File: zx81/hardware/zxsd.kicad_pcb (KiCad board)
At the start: 2 copper layers, 69.9 x 95.9 mm, 36 parts, among them J1 Micro_SD_Card, J2 ZX81_EXP, SW1 RESET, U1 74HCT32, U10 27C256, U11 KM62256CLP, U2 74HCT32, U3 74HCT00, U4 74HCT02, U5 74HCT163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

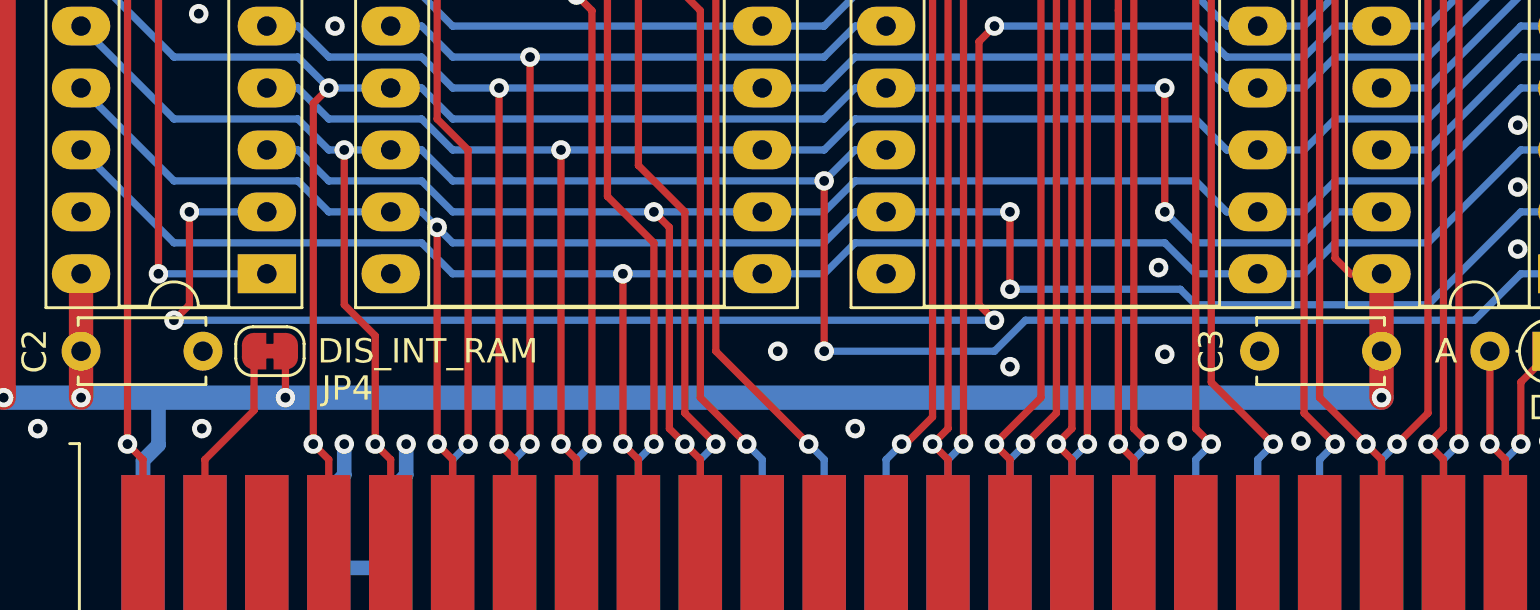
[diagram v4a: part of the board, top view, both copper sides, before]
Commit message: use real jumper for dis_int_ram
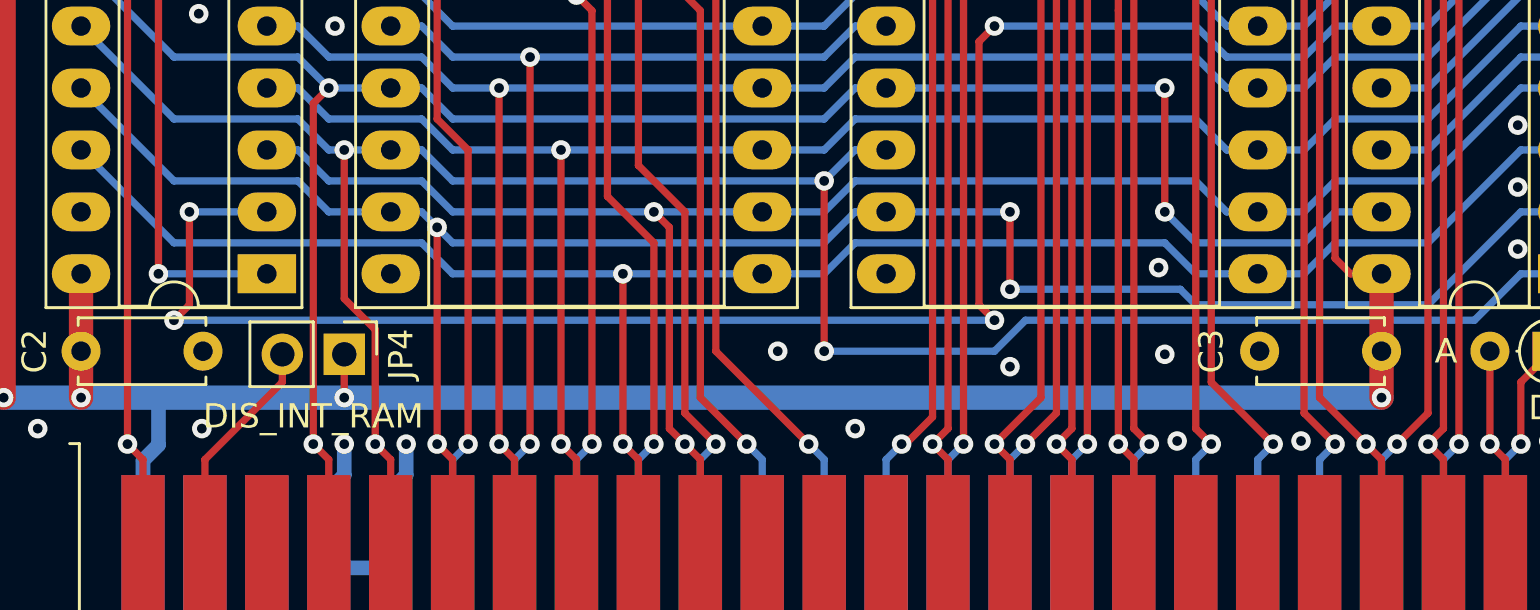
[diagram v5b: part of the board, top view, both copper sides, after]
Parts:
- JP4: footprint Jumper:SolderJumper-2_P1.3mm_Bridged_RoundedPad1.0x1.5mm -> Connector_PinHeader_2.54mm:PinHeader_1x02_P2.54mm_Vertical
- moved JP4 3.05 mm to (127.6, 126.5), turned to 270 degrees
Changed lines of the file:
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@@
     (add_net "Net-(J1-Pad5)")
     (add_net "Net-(J1-Pad8)")
+    (add_net "Net-(J2-Pad11a)")
+    (add_net "Net-(J2-Pad12a)")
+    (add_net "Net-(J2-Pad13a)")
+    (add_net "Net-(J2-Pad18a)")
+    (add_net "Net-(J2-Pad19a)")
+    (add_net "Net-(J2-Pad20a)")
+    (add_net "Net-(J2-Pad2b)")
+    (add_net "Net-(J2-Pad3a)")
+    (add_net "Net-(J2-Pad3b)")
     (add_net "Net-(JP1-Pad1)")
     (add_net "Net-(JP1-Pad3)")
@@
     (add_net "Net-(U11-Pad1)")
     (add_net "Net-(U2-Pad10)")
+    (add_net "Net-(U2-Pad11)")
     (add_net "Net-(U2-Pad4)")
     (add_net "Net-(U2-Pad8)")
     (add_net "Net-(U2-Pad9)")
     (add_net "Net-(U4-Pad1)")
+    (add_net "Net-(U4-Pad10)")
+    (add_net "Net-(U5-Pad13)")
+    (add_net "Net-(U5-Pad14)")
+    (add_net "Net-(U5-Pad15)")
+    (add_net "Net-(U6-Pad7)")
+    (add_net "Net-(U7-Pad9)")
+    (add_net "Net-(U8-Pad8)")
+  )
+  (module Connector_PinHeader_2.54mm:PinHeader_1x02_P2.54mm_Vertical (layer F.Cu)
+    (at 127.635 126.492 270)
+    (descr "Through hole straight pin header, 1x02, 2.54mm pitch, single row")
+    (tags "Through hole pin header THT 1x02 2.54mm single row")
+    (fp_text reference JP4 (at 0 -2.33 90) (layer F.SilkS)
+      (effects (font (size 1 1) (thickness 0.15)))
+    )
+    (fp_text value DIS_INT_RAM (at 0 4.87 90) (layer F.Fab)
+      (effects (font (size 1 1) (thickness 0.15)))
+    )
+    (fp_line (start 1.8 -1.8) (end -1.8 -1.8) (layer F.CrtYd) (width 0.05))
+    (fp_line (start 1.8 4.35) (end 1.8 -1.8) (layer F.CrtYd) (width 0.05))
+    (fp_line (start -1.8 4.35) (end 1.8 4.35) (layer F.CrtYd) (width 0.05))
+    (fp_line (start -1.8 -1.8) (end -1.8 4.35) (layer F.CrtYd) (width 0.05))
+    (fp_line (start -1.33 -1.33) (end 0 -1.33) (layer F.SilkS) (width 0.12))
+    (fp_line (start -1.33 0) (end -1.33 -1.33) (layer F.SilkS) (width 0.12))
+    (fp_line (start -1.33 1.27) (end 1.33 1.27) (layer F.SilkS) (width 0.12))
+    (fp_line (start 1.33 1.27) (end 1.33 3.87) (layer F.SilkS) (width 0.12))
+    (fp_line (start -1.33 1.27) (end -1.33 3.87) (layer F.SilkS) (width 0.12))
+    (fp_line (start -1.33 3.87) (end 1.33 3.87) (layer F.SilkS) (width 0.12))
+    (fp_line (start -1.27 -0.635) (end -0.635 -1.27) (layer F.Fab) (width 0.1))
+    (fp_line (start -1.27 3.81) (end -1.27 -0.635) (layer F.Fab) (width 0.1))
+    (fp_line (start 1.27 3.81) (end -1.27 3.81) (layer F.Fab) (width 0.1))
+    (fp_line (start 1.27 -1.27) (end 1.27 3.81) (layer F.Fab) (width 0.1))
+    (fp_line (start -0.635 -1.27) (end 1.27 -1.27) (layer F.Fab) (width 0.1))
+    (fp_text user %R (at 0 1.27) (layer F.Fab)
+      (effects (font (size 1 1) (thickness 0.15)))
+    )
+    (pad 2 thru_hole oval (at 0 2.54 270) (size 1.7 1.7) (drill 1) (layers *.Cu *.Mask)
+      (net 50 /nRAMCS_INT))
+    (pad 1 thru_hole rect (at 0 0 270) (size 1.7 1.7) (drill 1) (layers *.Cu *.Mask)
+      (net 1 +5V))
+    (model ${KISYS3DMOD}/Connector_PinHeader_2.54mm.3dshapes/PinHeader_1x02_P2.54mm_Vertical.wrl
+      (at (xyz 0 0 0))
+      (scale (xyz 1 1 1))
+      (rotate (xyz 0 0 0))
+    )
   )
   (module Package_DIP:DIP-14_W7.62mm_Socket_LongPads (layer F.Cu)
@@
     )
   )
-  (module Jumper:SolderJumper-2_P1.3mm_Bridged_RoundedPad1.0x1.5mm (layer F.Cu)
-    (at 124.587 126.365 180)
-    (descr "SMD Solder Jumper, 1x1.5mm, rounded Pads, 0.3mm gap, bridged with 1 copper strip")
-    (tags "solder jumper open")
-    (attr virtual)
-    (fp_text reference JP4 (at -3.175 -1.524) (layer F.SilkS)
-      (effects (font (size 1 1) (thickness 0.15)))
-    )
-    (fp_text value DIS_INT_RAM (at 0 1.9) (layer F.Fab)
-      (effects (font (size 1 1) (thickness 0.15)))
-    )
-    (fp_poly (pts (xy 0.25 -0.3) (xy -0.25 -0.3) (xy -0.25 0.3) (xy 0.25 0.3)) (layer F.Cu) (width 0))
-    (fp_line (start 1.65 1.25) (end -1.65 1.25) (layer F.CrtYd) (width 0.05))
-    (fp_line (start 1.65 1.25) (end 1.65 -1.25) (layer F.CrtYd) (width 0.05))
-    (fp_line (start -1.65 -1.25) (end -1.65 1.25) (layer F.CrtYd) (width 0.05))
-    (fp_line (start -1.65 -1.25) (end 1.65 -1.25) (layer F.CrtYd) (width 0.05))
-    (fp_line (start -0.7 -1) (end 0.7 -1) (layer F.SilkS) (width 0.12))
-    (fp_line (start 1.4 -0.3) (end 1.4 0.3) (layer F.SilkS) (width 0.12))
-    (fp_line (start 0.7 1) (end -0.7 1) (layer F.SilkS) (width 0.12))
-    (fp_line (start -1.4 0.3) (end -1.4 -0.3) (layer F.SilkS) (width 0.12))
-    (fp_arc (start -0.7 -0.3) (end -0.7 -1) (angle -90) (layer F.SilkS) (width 0.12))
-    (fp_arc (start -0.7 0.3) (end -1.4 0.3) (angle -90) (layer F.SilkS) (width 0.12))
-    (fp_arc (start 0.7 0.3) (end 0.7 1) (angle -90) (layer F.SilkS) (width 0.12))
-    (fp_arc (start 0.7 -0.3) (end 1.4 -0.3) (angle -90) (layer F.SilkS) (width 0.12))
-    (pad 1 smd custom (at -0.65 0 180) (size 1 0.5) (layers F.Cu F.Mask)
-      (net 1 +5V) (zone_connect 2)
-      (options (clearance outline) (anchor rect))
-      (primitives
-        (gr_circle (center 0 0.25) (end 0.5 0.25) (width 0))
-        (gr_circle (center 0 -0.25) (end 0.5 -0.25) (width 0))
-        (gr_poly (pts
-           (xy 0 -0.75) (xy 0.5 -0.75) (xy 0.5 0.75) (xy 0 0.75)) (width 0))
-      ))
-    (pad 2 smd custom (at 0.65 0 180) (size 1 0.5) (layers F.Cu F.Mask)
-      (net 50 /nRAMCS_INT) (zone_connect 2)
-      (options (clearance outline) (anchor rect))
-      (primitives
-        (gr_circle (center 0 0.25) (end 0.5 0.25) (width 0))
-        (gr_circle (center 0 -0.25) (end 0.5 -0.25) (width 0))
-        (gr_poly (pts
-           (xy 0 -0.75) (xy -0.5 -0.75) (xy -0.5 0.75) (xy 0 0.75)) (width 0))
-      ))
-  )
   (module Package_TO_SOT_THT:TO-92_Inline (layer F.Cu)
     (at 128.27 48.26)
@@
   )
   (gr_circle (center 165.735 48.895) (end 165.935 48.895) (layer F.SilkS) (width 0.15))
-  (gr_text DIS_INT_RAM (at 131.064 126.365) (layer F.SilkS)
+  (gr_text DIS_INT_RAM (at 126.365 129.032) (layer F.SilkS)
     (effects (font (size 1 1) (thickness 0.15)))
   )
@@
   (segment (start 128.905 50.8) (end 129.54 50.165) (width 0.6) (layer B.Cu) (net 1))
   (segment (start 113.665 128.27) (end 113.665 90.17) (width 1) (layer F.Cu) (net 1))
-  (segment (start 125.222 128.27) (end 170.18 128.27) (width 1) (layer B.Cu) (net 1))
-  (via (at 125.222 128.27) (size 0.8) (drill 0.4) (layers F.Cu B.Cu) (net 1))
-  (segment (start 120.015 128.27) (end 125.222 128.27) (width 1) (layer B.Cu) (net 1))
-  (segment (start 125.222 126.38) (end 125.237 126.365) (width 0.3) (layer F.Cu) (net 1))
-  (segment (start 125.222 128.27) (end 125.222 126.38) (width 0.3) (layer F.Cu) (net 1))
   (segment (start 116.84 69.85) (end 122.555 69.85) (width 0.3) (layer B.Cu) (net 1))
   (via (at 122.555 69.85) (size 0.8) (drill 0.4) (layers F.Cu B.Cu) (net 1))
@@
   (via (at 165.1 85.09) (size 0.8) (drill 0.4) (layers F.Cu B.Cu) (net 1))
   (segment (start 165.1 85.09) (end 165.1 86.995) (width 1) (layer F.Cu) (net 1))
+  (segment (start 120.015 128.27) (end 127.635 128.27) (width 1) (layer B.Cu) (net 1))
+  (via (at 127.635 128.27) (size 0.8) (drill 0.4) (layers F.Cu B.Cu) (net 1))
+  (segment (start 127.635 128.27) (end 170.18 128.27) (width 1) (layer B.Cu) (net 1))
+  (segment (start 127.635 128.27) (end 127.635 126.492) (width 0.3) (layer F.Cu) (net 1))
   (via (at 153.67 67.31) (size 0.8) (drill 0.4) (layers F.Cu B.Cu) (net 2))
   (via (at 130.175 130.175) (size 0.8) (drill 0.4) (layers F.Cu B.Cu) (net 2))
@@
   (segment (start 120.65 116.84) (end 116.84 113.03) (width 0.3) (layer B.Cu) (net 18))
   (via (at 147.32 119.38) (size 0.8) (drill 0.4) (layers F.Cu B.Cu) (net 18))
-  (segment (start 128.905 130.175) (end 128.905 125.73) (width 0.3) (layer F.Cu) (net 18))
-  (segment (start 127.635 124.46) (end 127.635 118.11) (width 0.3) (layer F.Cu) (net 18))
-  (segment (start 128.905 125.73) (end 127.635 124.46) (width 0.3) (layer F.Cu) (net 18))
   (segment (start 155.575 125.095) (end 154.305 126.365) (width 0.3) (layer B.Cu) (net 18))
   (via (at 147.32 126.365) (size 0.8) (drill 0.4) (layers F.Cu B.Cu) (net 18))
@@
   (segment (start 175.895 123.19) (end 177.8 123.19) (width 0.3) (layer B.Cu) (net 18))
   (segment (start 173.99 125.095) (end 175.895 123.19) (width 0.3) (layer B.Cu) (net 18))
+  (segment (start 127.635 124.206) (end 127.635 118.11) (width 0.3) (layer F.Cu) (net 18))
+  (segment (start 128.905 130.175) (end 128.905 125.476) (width 0.3) (layer F.Cu) (net 18))
+  (segment (start 128.905 125.476) (end 127.635 124.206) (width 0.3) (layer F.Cu) (net 18))
   (segment (start 163.83 118.11) (end 162.56 116.84) (width 0.3) (layer B.Cu) (net 19))
   (segment (start 165.1 118.11) (end 163.83 118.11) (width 0.3) (layer B.Cu) (net 19))
@@
   (via (at 126.365 83.82) (size 0.8) (drill 0.4) (layers F.Cu B.Cu) (net 49))
   (segment (start 152.4 83.82) (end 126.365 83.82) (width 0.3) (layer B.Cu) (net 49))
+  (segment (start 125.222 126.38) (end 125.237 126.365) (width 0.3) (layer F.Cu) (net 50))
   (segment (start 121.92 135.255) (end 121.92 130.81) (width 0.3) (layer F.Cu) (net 50))
-  (segment (start 123.937 128.793) (end 123.937 126.365) (width 0.3) (layer F.Cu) (net 50))
-  (segment (start 121.92 130.81) (end 123.937 128.793) (width 0.3) (layer F.Cu) (net 50))
+  (segment (start 125.095 127.635) (end 125.095 126.492) (width 0.3) (layer F.Cu) (net 50))
+  (segment (start 121.92 130.81) (end 125.095 127.635) (width 0.3) (layer F.Cu) (net 50))
   (segment (start 170.18 115.57) (end 172.085 115.57) (width 0.3) (layer B.Cu) (net 51))
   (segment (start 172.085 115.57) (end 175.895 111.76) (width 0.3) (layer B.Cu) (net 51))

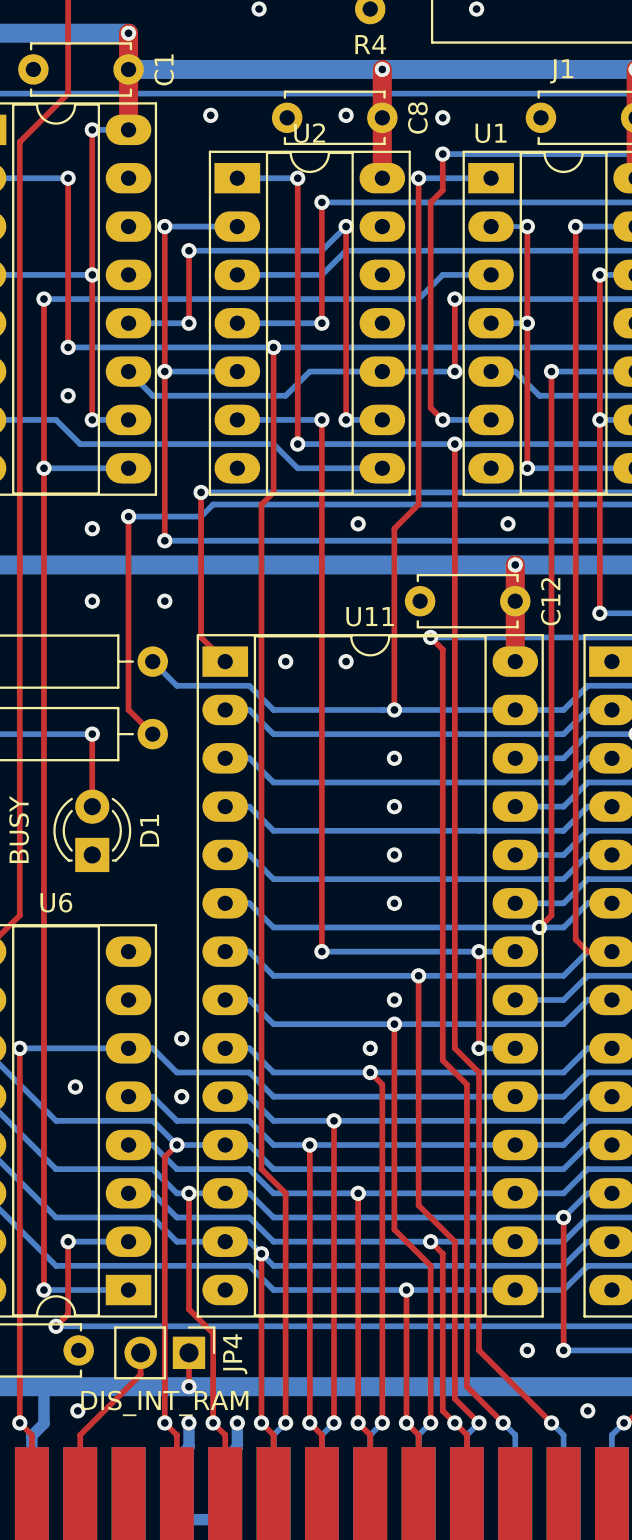
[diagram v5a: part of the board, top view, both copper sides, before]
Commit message: JP4 switches between internal/expansion board RAM
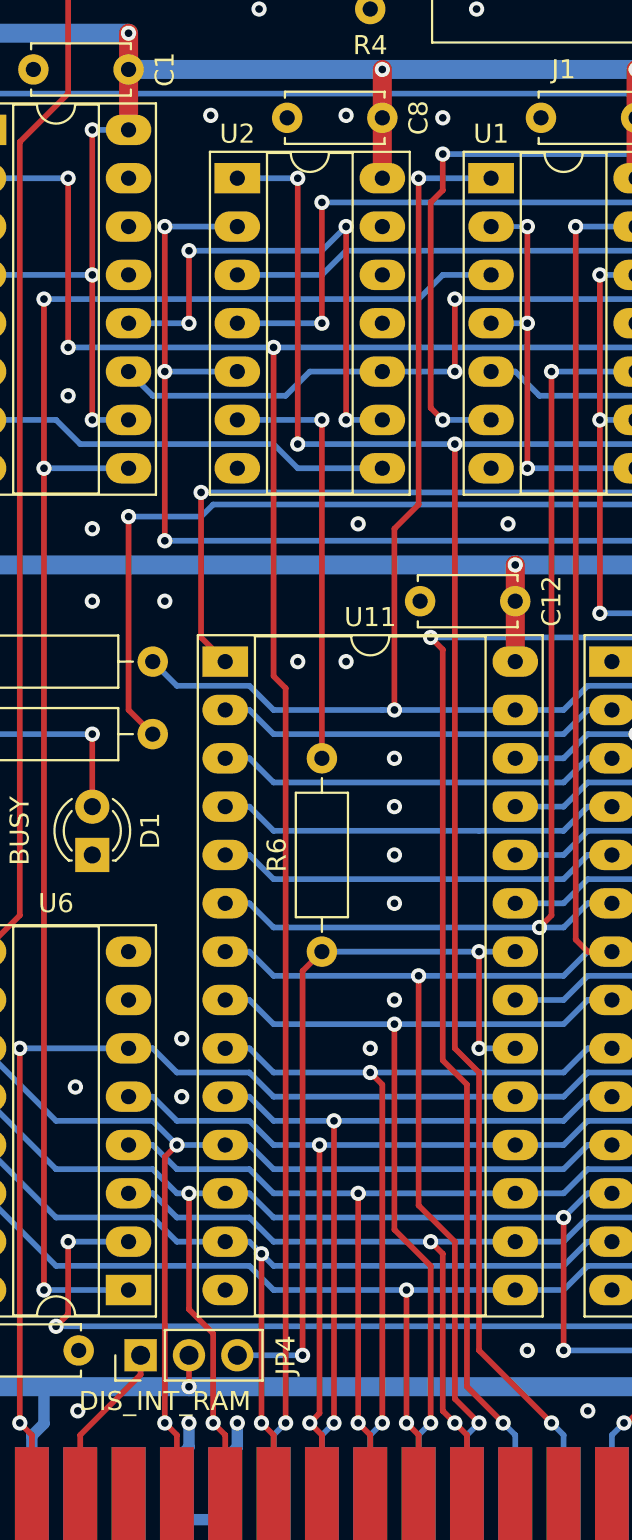
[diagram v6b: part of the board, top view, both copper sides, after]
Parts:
- added R6: 680R, Resistor_THT:R_Axial_DIN0207_L6.3mm_D2.5mm_P10.16mm_Horizontal, F.Cu at (134.6, 105.4)
- JP4: footprint Connector_PinHeader_2.54mm:PinHeader_1x02_P2.54mm_Vertical -> Connector_PinHeader_2.54mm:PinHeader_1x03_P2.54mm_Vertical
- moved JP4 2.54 mm to (125.1, 126.6), turned to 90 degrees
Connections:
- JP4 pad 1: +5V -> /nRAMCS_INT
- JP4 pad 2: /nRAMCS_INT -> +5V
- U2 pad 6: /nCS_RAM -> Net-(R6-Pad2)
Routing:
- net Net-(R6-Pad2): track 0.00 -> 22.2 mm, vias 0 -> 1
- net /nCS_RAM: track 49.5 -> 42.2 mm, vias 4 -> 3
- net /CLK: track 119.7 -> 119.2 mm

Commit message: migrated to KiCAD 6.0
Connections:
- net +3V3 renamed +3.3V
- J2 pad 11a: (no net) -> unconnected-(J2-Pad11a)
- J2 pad 12a: (no net) -> unconnected-(J2-Pad12a)
- J2 pad 13a: (no net) -> unconnected-(J2-Pad13a)
- J2 pad 18a: (no net) -> unconnected-(J2-Pad18a)
- J2 pad 19a: (no net) -> unconnected-(J2-Pad19a)
- J2 pad 20a: (no net) -> unconnected-(J2-Pad20a)
- J2 pad 2b: (no net) -> unconnected-(J2-Pad2b)
- J2 pad 3a: (no net) -> unconnected-(J2-Pad3a)
- J2 pad 3b: (no net) -> unconnected-(J2-Pad3b)
- U2 pad 11: (no net) -> unconnected-(U2-Pad11)
- U4 pad 10: (no net) -> unconnected-(U4-Pad10)
- U5 pad 13: (no net) -> unconnected-(U5-Pad13)
- U5 pad 14: (no net) -> unconnected-(U5-Pad14)
- U5 pad 15: (no net) -> unconnected-(U5-Pad15)
- U6 pad 7: (no net) -> unconnected-(U6-Pad7)
- U7 pad 9: (no net) -> unconnected-(U7-Pad9)
- U8 pad 8: (no net) -> unconnected-(U8-Pad8)
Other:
- net class Default removed
